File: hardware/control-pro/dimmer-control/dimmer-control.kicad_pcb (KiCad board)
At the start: 2 copper layers, 69.1 x 53.8 mm, 10 parts, among them J1 Output, J2 INPUT

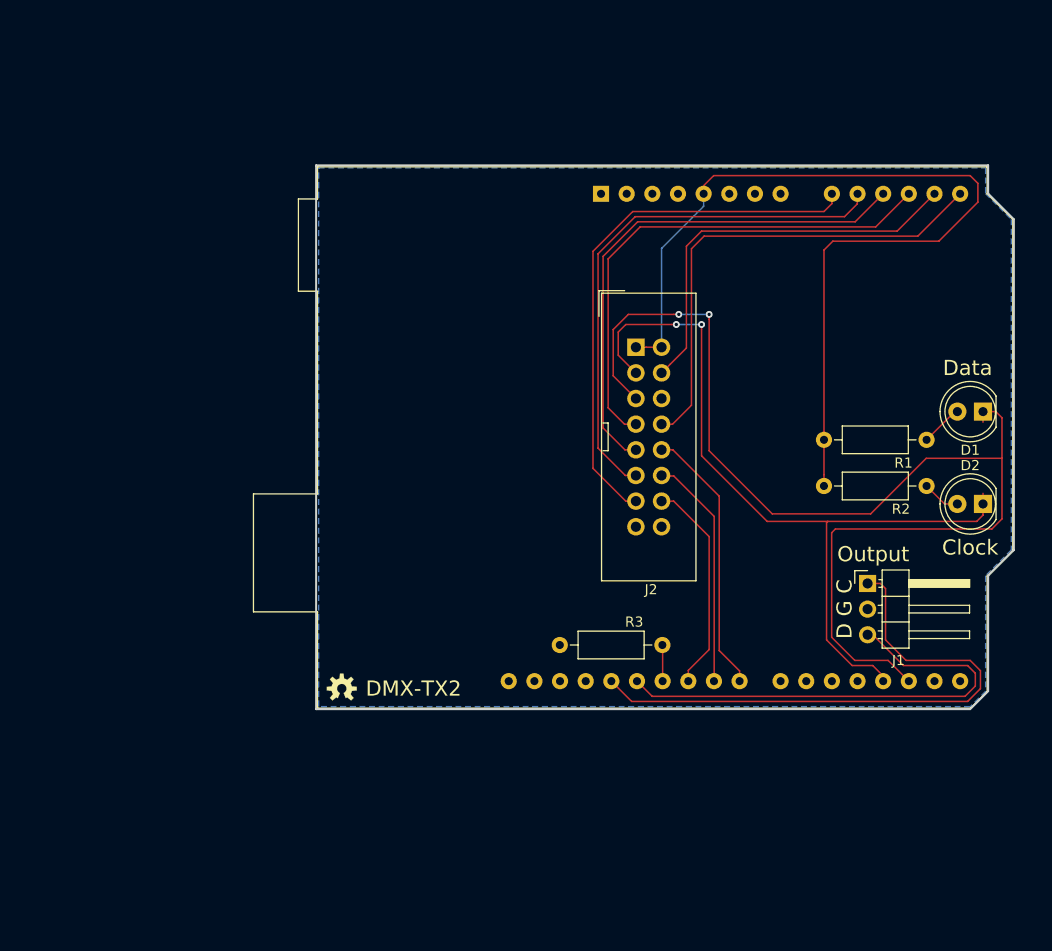
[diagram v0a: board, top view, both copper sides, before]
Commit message: Users/sparky/control pro v1.3 (#18)
* DMX-TX2 V1.1:
- Fixed shield footprint
- Moved Clock LED to avoid Arduino ICSP connector.
- Relabeled the clock fast and slow LED connections in the
  schematic to match the board layout.
- Added Fcu power plane
- Redid Fcu layout
- Added rounded corners

* Refactor Control-Pro:
- Rename all dimmers to dim1-4 (instead of dim0-3)
- Split control-pro into 2 smaller board to save on board cost
- clock-control/faceplate only has clock controls
- dimmer-control/faceplate only has dimmer controls
- both control-pro boards have 2 ribbon cable connectors

* TX2:
- Added buffer to drive LEDs
- Added decoupling capacitors
- Fixed dimmer traces on PCB

DMX-CPC*:
- Switched to horizontal 16 pin connectors since vertical was too tall with a cable plugged in
- Swapped the clock speed and step switches to match the order on the TX1
- Swapped the data and clock LEDs to match the order on the TX1

DMX-CPD*:
- Split dimmer controls out to its own PCB
- Added 2nd 16 pin connector to daisy chain with DMX-CPC*.
- Switched to horizontal 16 pin connectors since vertical was too tall with a cable plugged in

Updated readmes with parts, board links.

* Remove Control Pro transmitter in favor of Transmitter IO Interface (DMX-TX2).
Add status information.

* Fix status badges.

* Output local gerbers (ignored)

* Add copper pours to faceplates.

* Update nets for copper pours on control faceplate.

* Add Tx-IO:
- Switch to 74LS07 for Led driver
- Add pulldown resistor for discovery
- Add silkscreen values

Discovery:
- Make use of new Tx-IO pulldown resistor

Transmitter
- Fix bugs related to Control Pro

---------

Co-authored-by: SparkyBobo <sparky@crazygiraffesoftware.com>
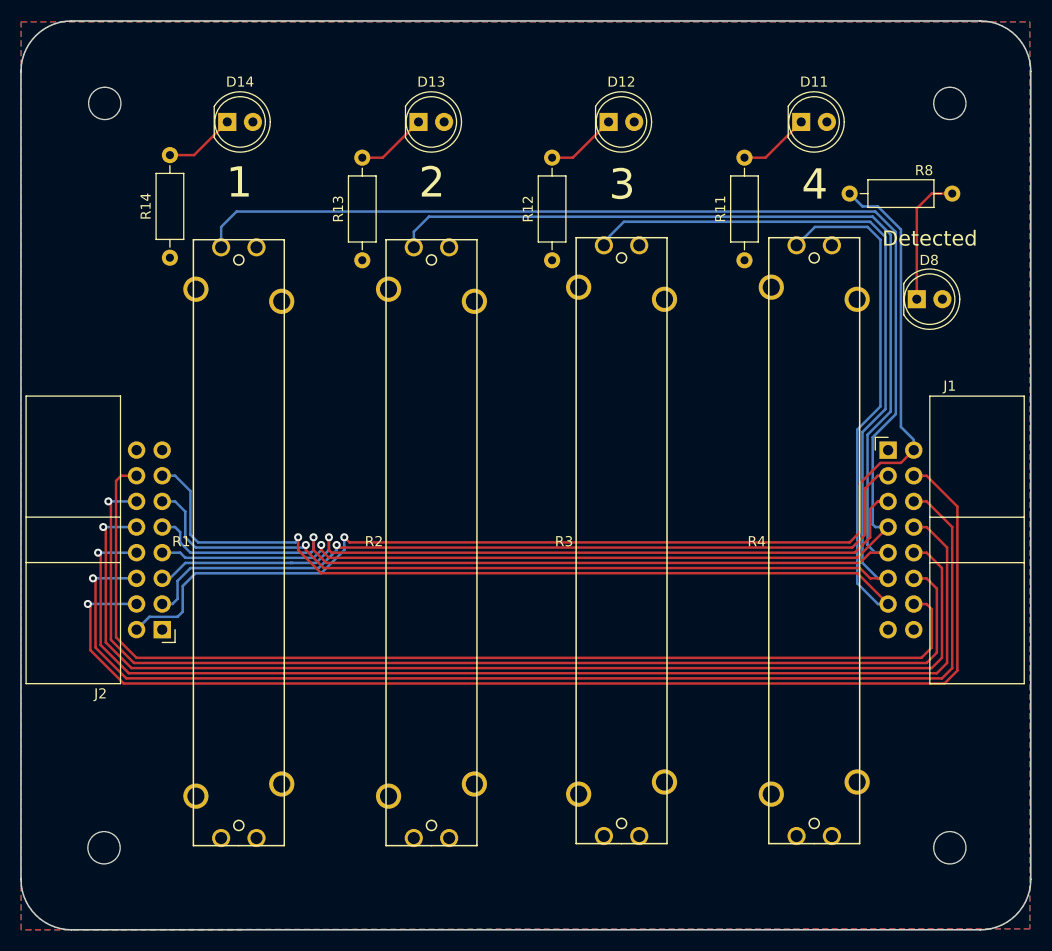
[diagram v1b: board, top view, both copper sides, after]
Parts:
- removed the ? at (118.9, 114.8)
- removed A1: Arduino_UNO_R3, Module:Arduino_UNO_R3
- removed D1: DATA, LED_THT:LED_D5.0mm
- removed D2: CLOCK, LED_THT:LED_D5.0mm
- added ?: , footprints:OSHW-LOGO-S, B.Cu at (171.7, 135.9)
- added D11: DIM4, LED_THT:LED_D5.0mm, F.Cu at (164.4, 58.7)
- added D12: DIM3, LED_THT:LED_D5.0mm, F.Cu at (145.3, 58.7)
- added D13: DIM2, LED_THT:LED_D5.0mm, F.Cu at (126.5, 58.7)
- added D14: DIM1, LED_THT:LED_D5.0mm, F.Cu at (107.5, 58.7)
- added D8: LED, LED_THT:LED_D5.0mm, F.Cu at (175.8, 76.2)
- added MH1: MountingHole, MountingHole:MountingHole_3.2mm_M3, F.Cu at (95.4, 56.9)
- added MH2: MountingHole, MountingHole:MountingHole_3.2mm_M3, F.Cu at (95.3, 130.6)
- added MH3: MountingHole, MountingHole:MountingHole_3.2mm_M3, F.Cu at (179.1, 56.9)
- added MH4: MountingHole, MountingHole:MountingHole_3.2mm_M3, F.Cu at (179.1, 130.6)
- added R11: 330, Resistor_THT:R_Axial_DIN0207_L6.3mm_D2.5mm_P10.16mm_Horizontal, F.Cu at (158.8, 72.4)
- added R12: 330, Resistor_THT:R_Axial_DIN0207_L6.3mm_D2.5mm_P10.16mm_Horizontal, F.Cu at (139.7, 72.4)
- added R13: 330, Resistor_THT:R_Axial_DIN0207_L6.3mm_D2.5mm_P10.16mm_Horizontal, F.Cu at (120.9, 72.4)
- added R14: 330, Resistor_THT:R_Axial_DIN0207_L6.3mm_D2.5mm_P10.16mm_Horizontal, F.Cu at (101.9, 72.1)
- added R4: 10k, footprints:BOURNS_PTA4543, F.Cu at (165.7, 100.2)
- added R8: 330, Resistor_THT:R_Axial_DIN0207_L6.3mm_D2.5mm_P10.16mm_Horizontal, F.Cu at (169.2, 65.8)
- J1: value Output -> OUTPUT; footprint Connector_PinHeader_2.54mm:PinHeader_1x03_P2.54mm_Horizontal -> Connector_IDC:IDC-Header_2x08_P2.54mm_Horizontal
- J2: footprint Connector_IDC:IDC-Header_2x08_P2.54mm_Vertical -> Connector_IDC:IDC-Header_2x08_P2.54mm_Horizontal
- R1, R2, R3: value 330 -> 10k; footprint Resistor_THT:R_Axial_DIN0207_L6.3mm_D2.5mm_P10.16mm_Horizontal -> footprints:BOURNS_PTA4543
- moved R1 58.8 mm to (108.7, 100.4), turned to 180 degrees
- moved J2 54.6 mm to (101.1, 109.0), turned to 180 degrees
- moved R2 39.3 mm to (127.8, 100.4), turned to 180 degrees
- moved G*** 38.7 mm to (149.7, 134.9)
- moved J1 13.4 mm to (173.0, 91.2)
- moved R3 11.1 mm to (146.6, 100.2)
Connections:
- J1 pad 1: /RXCLK -> +5V
- J1 pad 2: GND -> /~HWD_DT
- J1 pad 3: /RX -> /~CLOCK
- J2 pad 10: /~CLK_SLO -> /~CLK_STEP
- J2 pad 11: /A1 -> /DIM3
- J2 pad 12: /~CLK_FST -> /~CLK_SLO
- J2 pad 13: /A0 -> /DIM4
- J2 pad 14: /~HWD_DT -> /~CLK_FST
- J2 pad 2: +5V -> /~HWD_DT
- J2 pad 4: /A4 -> /SPD_HI
- J2 pad 6: GND -> /SPD_WIPER
- J2 pad 7: /A3 -> /DIM1
- J2 pad 8: /A5 -> /SPD_LO
- J2 pad 9: /A2 -> /DIM2
- R1 pad 2: Net-(D1-Pad2) -> /DIM1
- R2 pad 2: Net-(D2-Pad2) -> /DIM2
- R3 pad 1: Net-(A1-Pad26) -> +5V
- R3 pad 2: GND -> /DIM3
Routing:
- net /DIM1: track 0.00 -> 176.8 mm, vias 0 -> 1
- net /DIM2: track 0.00 -> 161.3 mm, vias 0 -> 1
- net /DIM3: track 0.00 -> 143.1 mm, vias 0 -> 1
- net /DIM4: track 0.00 -> 129.4 mm, vias 0 -> 1
- net /SPD_HI: track 0.00 -> 119.1 mm, vias 0 -> 1
- net /SPD_WIPER: track 0.00 -> 116.6 mm, vias 0 -> 1
- net /SPD_LO: track 0.00 -> 114.0 mm, vias 0 -> 1
- net /~CLK_STEP: track 0.00 -> 111.4 mm, vias 0 -> 1
- net /~HWD_DT: track 21.3 -> 118.7 mm, vias 0 -> 1
- net +5V: track 90.6 -> 0.08 mm
- net /~CLK_FST: track 23.2 -> 105.6 mm
- net /~CLK_SLO: track 26.8 -> 108.8 mm, vias 0 -> 1
- net /RXCLK: track 57.4 -> 0.00 mm
- net /A0: track 53.7 -> 0.00 mm
- net /A1: track 52.9 -> 0.00 mm
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- added copper zone on F.Cu, net +5V
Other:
- board size 69.1 x 53.8 mm -> 100 x 90 mm
- net class Default: clearance 0.1524 -> 0.2; trace_width 0.1524 -> 0.25; via_dia 0.6858 -> 0.8; via_drill 0.3302 -> 0.4
- rule trace_clearance: 0.1524 -> 0.2
- rule trace_min: 0.1524 -> 0.2
- rule via_min_drill: 0.254 -> 0.3
- rule via_min_size: 0.508 -> 0.4
- board text added: "1"
- board text added: "2"
- board text added: "3"
- board text added: "4"
- board text added: "DMX-CPDB, Rev 1.3 Crazy Giraffe Software"
- board text added: "Detected"
- board text removed: "Clock"
- board text removed: "D G C"
- board text removed: "DMX-TX2"
- board text removed: "DMX-TX2, Rev 1.0 Crazy Giraffe Software"
- board text removed: "Data"
- board text removed: "Output"

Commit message: Rebrand to Sparky Bobo Designs
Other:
- board text added: "DMX-CPDB, Rev 1.3 Sparky Bobo Designs"
- board text removed: "DMX-CPDB, Rev 1.3 Crazy Giraffe Software"
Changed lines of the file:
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@@
     (date 2023-12-04)
     (rev 1.3)
-    (company "Crazy Giraffe Software")
+    (company "Sparky Bobo Designs")
     (comment 2 "Designed by: SparkyBobo")
     (comment 3 https://creativecommons.org/licenses/by-sa/4.0/)
@@
     (effects (font (size 1.5 1.5) (thickness 0.3)))
   )
-  (gr_text "DMX-CPDB, Rev 1.3\nCrazy Giraffe Software" (at 160.414 136.102) (layer B.SilkS)
+  (gr_text "DMX-CPDB, Rev 1.3\nSparky Bobo Designs" (at 160.414 136.102) (layer B.SilkS)
     (effects (font (size 1 1) (thickness 0.15)) (justify mirror))
   )
